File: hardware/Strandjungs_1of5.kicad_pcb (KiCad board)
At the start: 2 copper layers, 62.2 x 80.4 mm, 54 parts, among them J1 Screw_Terminal_01x02, J10 Conn_01x02, J11 Conn_01x02, J12 Conn_01x02, J2 Screw_Terminal_01x02, J3 Screw_Terminal_01x02, J4 Screw_Terminal_01x02, J5 Screw_Terminal_01x02, J6 Screw_Terminal_01x02, J7 Screw_Terminal_01x02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

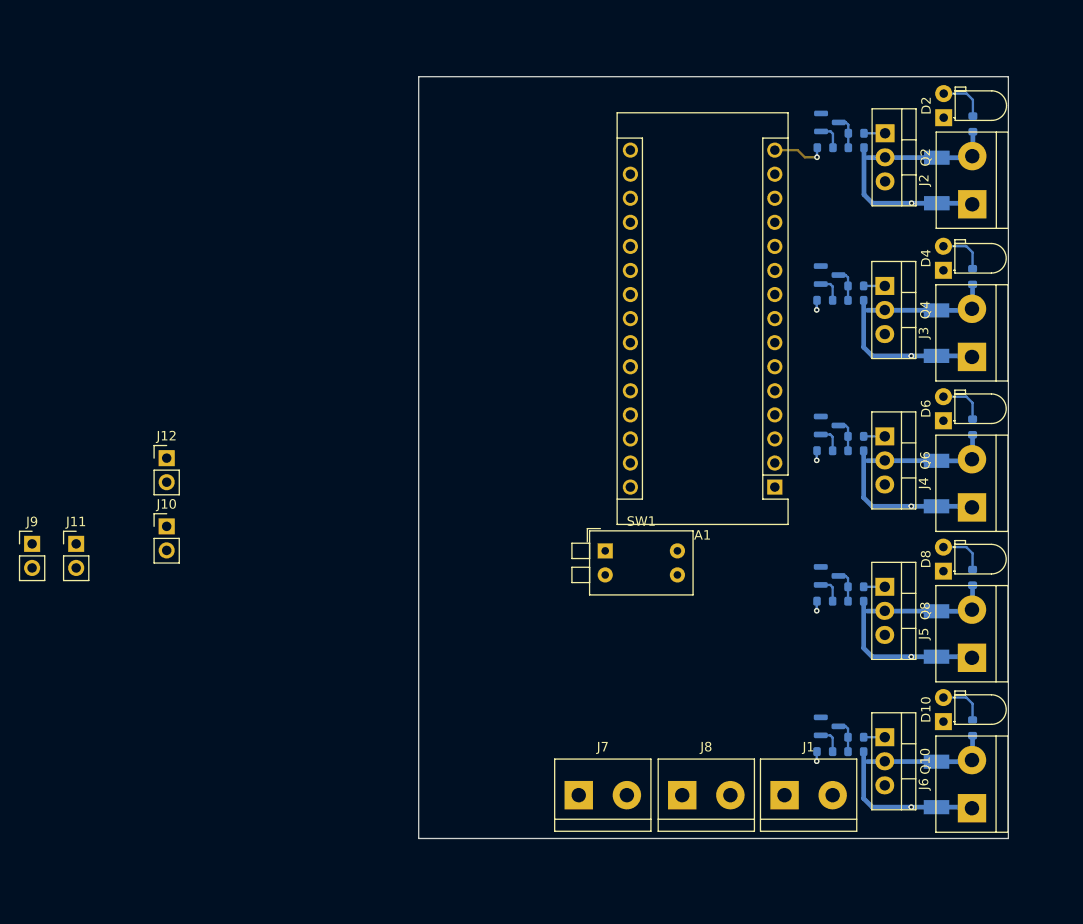
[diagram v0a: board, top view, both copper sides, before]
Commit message: first iteration of layout almost done
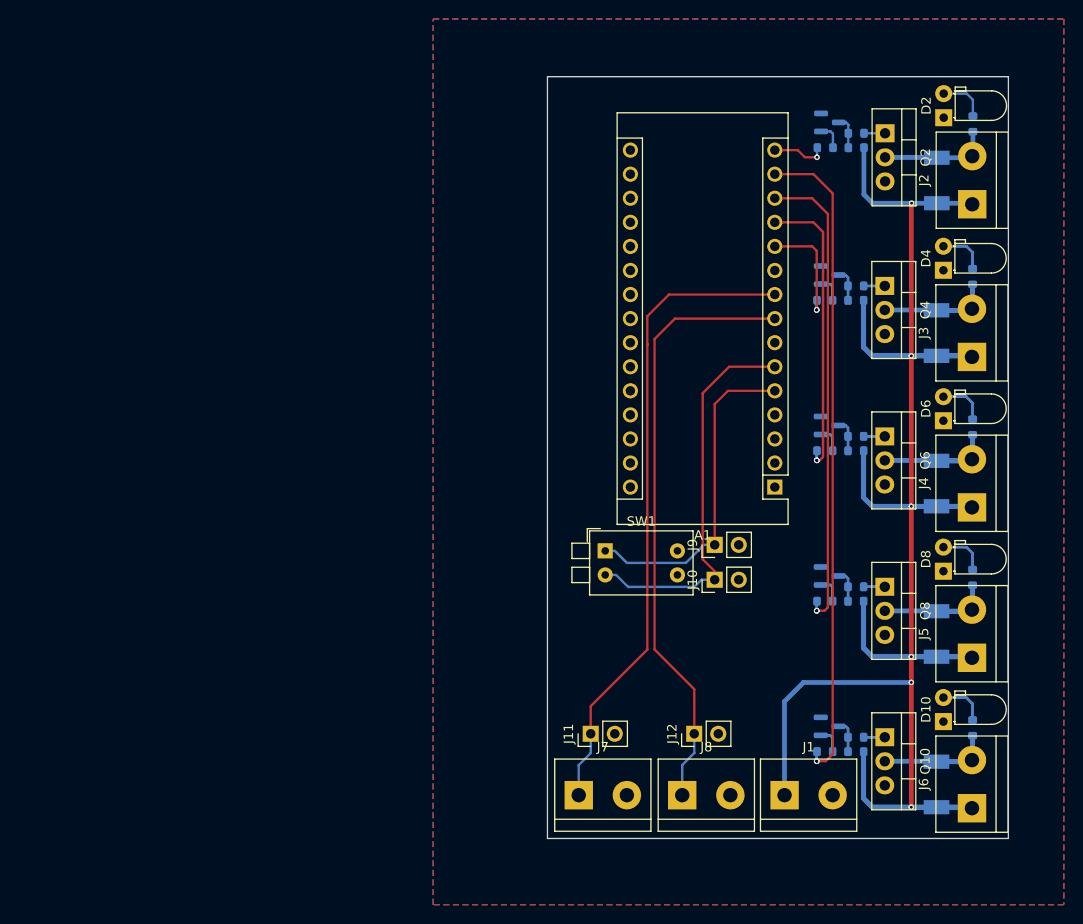
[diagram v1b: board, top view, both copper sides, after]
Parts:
- moved J9 72.0 mm to (31.6, -111.5), turned to 90 degrees
- moved J12 62.8 mm to (29.5, -91.6), turned to 90 degrees
- moved J10 58.1 mm to (31.6, -107.8), turned to 90 degrees
- moved J11 57.9 mm to (18.5, -91.6), turned to 90 degrees
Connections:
- A1 pad 8: /RESET -> /TRIGGER
- A1 pad 9: /TRIGGER -> /RESET
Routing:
- net +12V: track 0.00 -> 239.1 mm, vias 0 -> 6
- net /SWITCH4: track 1.01 -> 70.1 mm, vias 1 -> 2
- net /RESET: track 0.00 -> 68.1 mm
- net /TRIGGER: track 0.00 -> 64.0 mm
- net /SWITCH3: track 1.01 -> 51.2 mm, vias 1 -> 2
- net /SEL_1: track 0.00 -> 41.4 mm
- net /SEL_0: track 0.00 -> 34.6 mm
- net /SWITCH2: track 1.01 -> 32.1 mm, vias 1 -> 2
- net /Channel 0/MAG_RTN: track 30.5 -> 11.9 mm, vias 1 -> 0
- net /Channel 4/MAG_RTN: track 30.5 -> 18.3 mm, vias 1 -> 0
- net /Channel 3/MAG_RTN: track 30.5 -> 18.3 mm, vias 1 -> 0
- net /Channel 2/MAG_RTN: track 30.5 -> 18.3 mm, vias 1 -> 0
- net /Channel 1/MAG_RTN: track 30.5 -> 18.3 mm, vias 1 -> 0
- net /SWITCH1: track 1.01 -> 12.9 mm, vias 1 -> 2
- net Net-(D4-Pad2): track 4.94 -> 9.88 mm
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- added copper zone on B.Cu, net GND
- added copper zone on F.Cu, net GND
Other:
- board size 62.2 x 80.4 mm -> 48.6 x 80.4 mm

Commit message: added 7805 as voltage regulator
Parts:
- added R16: dnp, Resistor_SMD:R_0603_1608Metric, B.Cu at (18.9, -117.6)
- added REF**: Symbol_GNU-GPL_CopperTop_Small, Symbol:Symbol_GNU-GPL_CopperTop_Small, F.Cu at (29.2, -156.6)
- added REF**: KiCad-Logo2_6mm_SilkScreen, Symbol:KiCad-Logo2_6mm_SilkScreen, F.Cu at (42.1, -127.0)
- added U1: L7805, Package_TO_SOT_THT:TO-220-3_Vertical, F.Cu at (39.0, -96.3)
- added kibuzzard-62B9DC86: G***, kibuzzard-62B9DC86, F.Cu at (30.9, -95.1)
- added kibuzzard-62B9DCAD: G***, kibuzzard-62B9DCAD, F.Cu at (19.8, -95.2)
- added kibuzzard-62B9DCC5: G***, kibuzzard-62B9DCC5, F.Cu at (50.8, -145.8)
- added kibuzzard-62B9DCD6: G***, kibuzzard-62B9DCD6, F.Cu at (51.0, -129.7)
- added kibuzzard-62B9DCE2: G***, kibuzzard-62B9DCE2, F.Cu at (51.0, -113.8)
- added kibuzzard-62B9DCF0: G***, kibuzzard-62B9DCF0, F.Cu at (51.0, -97.8)
- added kibuzzard-62B9DD05: G***, kibuzzard-62B9DD05, F.Cu at (50.9, -82.0)
- added kibuzzard-62B9DD70: G***, kibuzzard-62B9DD70, F.Cu at (21.5, -104.1)
- moved J10 2.16 mm to (29.5, -107.7)
- moved J9 2.16 mm to (29.5, -111.4)
- moved SW1 2.16 mm to (17.9, -110.7)
- moved A1 1.14 mm to (36.8, -117.6)
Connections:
- A1 pad 27: unconnected-(A1-Pad27) -> +5V
- A1 pad 30: unconnected-(A1-Pad30) -> Net-(A1-Pad30)
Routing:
- net +5V: track 0.00 -> 39.9 mm
- net +12V: track 239.1 -> 212.2 mm
- net /Channel 1/MAG_RTN: track 18.3 -> 11.5 mm
- net /Channel 4/MAG_RTN: track 18.3 -> 11.5 mm
- net /Channel 3/MAG_RTN: track 18.3 -> 11.5 mm
- net /Channel 2/MAG_RTN: track 18.3 -> 11.5 mm
- net Net-(D4-Pad2): track 9.88 -> 4.94 mm
- net Net-(D8-Pad2): track 9.88 -> 4.94 mm
- net Net-(D6-Pad2): track 9.88 -> 4.94 mm
- net Net-(D10-Pad2): track 9.88 -> 4.94 mm
- net Net-(Q9-Pad3): track 7.05 -> 3.52 mm
- net Net-(Q5-Pad3): track 7.05 -> 3.52 mm
- net Net-(Q7-Pad3): track 7.05 -> 3.52 mm
- net Net-(Q3-Pad3): track 7.05 -> 3.52 mm
- net /TRIGGER: track 64.0 -> 67.4 mm
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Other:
- board text added: "Strandjungs Reaction Game"
- board text added: "https://github.com/JochiSt/Strandjungs_ReactionGame"

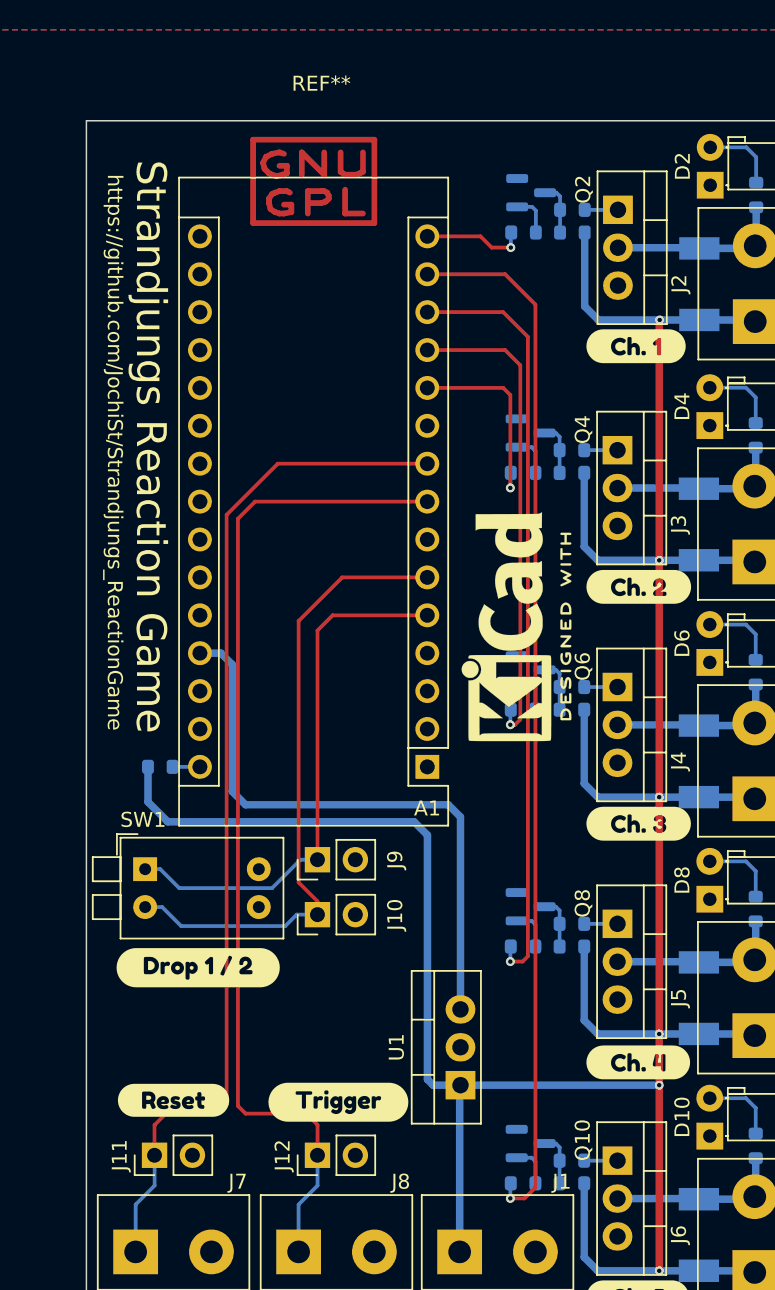
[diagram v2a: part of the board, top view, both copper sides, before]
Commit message: updated layout
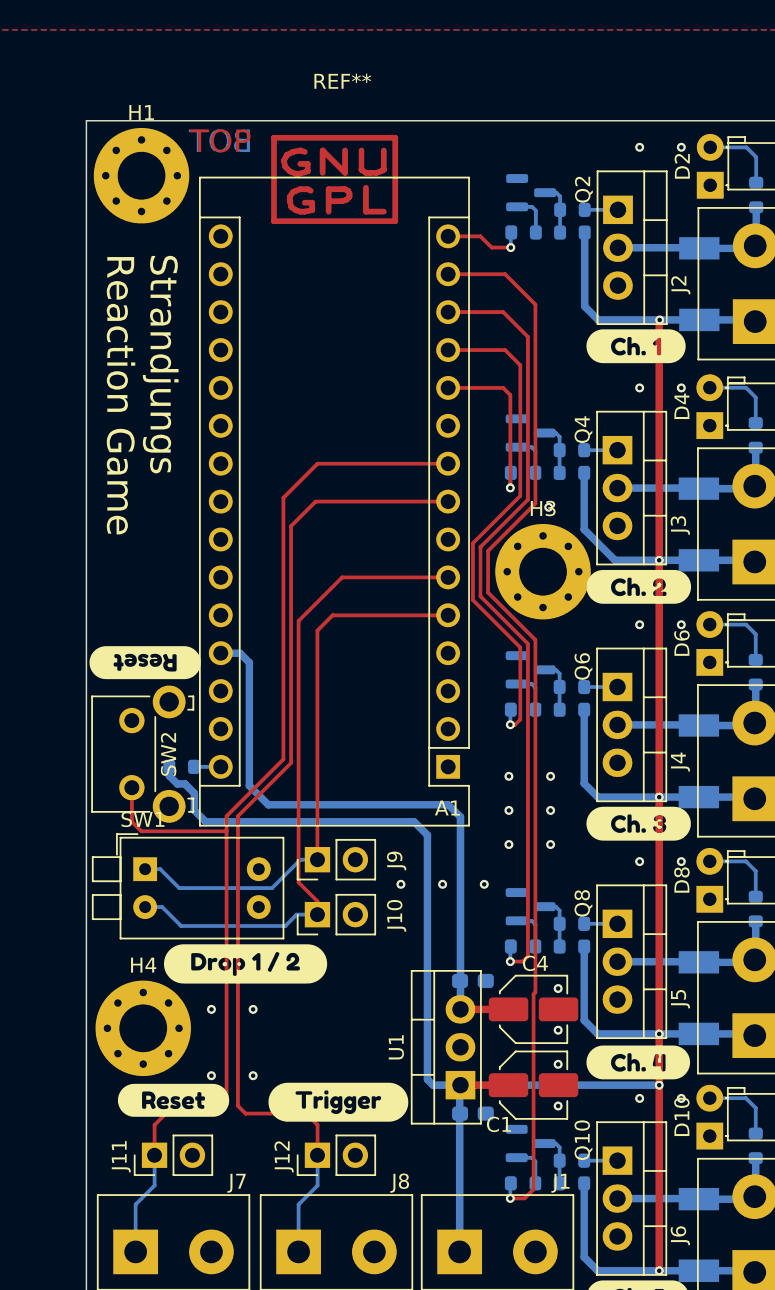
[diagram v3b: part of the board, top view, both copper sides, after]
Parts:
- added C1: 1uF, Capacitor_SMD:C_Elec_4x5.4, F.Cu at (43.9, -96.3)
- added C2: 100n, Capacitor_SMD:C_0603_1608Metric_Pad1.08x0.95mm_HandSolder, B.Cu at (39.9, -94.4)
- added C3: 100n, Capacitor_SMD:C_0603_1608Metric_Pad1.08x0.95mm_HandSolder, B.Cu at (39.9, -103.3)
- added C4: 10uF, Capacitor_SMD:C_Elec_4x5.4, F.Cu at (43.9, -101.3)
- added G***: LOGO, MadeByJochen:MadeByJochen_10x10, B.Cu at (30.9, -121.7)
- added H1: MountingHole_Pad, MountingHole:MountingHole_3.2mm_M3_Pad_Via, F.Cu at (17.7, -157.2)
- added H3: MountingHole_Pad, MountingHole:MountingHole_3.2mm_M3_Pad_Via, F.Cu at (44.6, -130.7)
- added H4: MountingHole_Pad, MountingHole:MountingHole_3.2mm_M3_Pad_Via, F.Cu at (17.8, -100.1)
- added SW2: SW_Push, Button_Switch_THT:SW_Tactile_SKHH_Angled, F.Cu at (17.0, -116.2)
- added kibuzzard-62B9DCAD: G***, kibuzzard-62B9DCAD, F.Cu at (17.9, -124.6)
- REF**: moved to B.Cu
- moved REF** 22.6 mm to (31.6, -146.9)
- moved kibuzzard-62B9DD70 3.19 mm to (24.6, -104.4)
- moved R16 1.43 mm to (20.4, -117.6)
- moved REF** 1.40 mm to (30.6, -156.7)
- moved A1 1.40 mm to (38.2, -117.6)
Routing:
- net /RESET: track 68.7 -> 77.5 mm
- net +5V: track 39.9 -> 41.6 mm
- net /SEL_0: track 35.9 -> 37.4 mm
- net /SWITCH1: track 13.0 -> 11.6 mm
- net /SWITCH0: track 6.92 -> 5.52 mm
- net /SEL_1: track 42.4 -> 43.8 mm
- net /SWITCH4: track 70.3 -> 71.5 mm
- net /SWITCH2: track 32.2 -> 33.5 mm
- net /SWITCH3: track 51.3 -> 52.5 mm
- net /TRIGGER: track 67.4 -> 66.4 mm
- net +12V: track 212.2 -> 212.9 mm
- net GND: vias 0 -> 28
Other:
- board text added: "BOT"
- board text added: "JS 06/2022"
- board text added: "TOP"

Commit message: updated AISLER project ID
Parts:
- moved A1 236.6 mm to (151.2, 90.3)
- moved C1 236.6 mm to (156.9, 111.6)
- moved C2 236.6 mm to (152.8, 113.5)
- moved C3 236.6 mm to (152.8, 104.6)
- moved C4 236.6 mm to (156.9, 106.6)
- moved D1 236.6 mm to (168.0, 57.9)
- moved D10 236.6 mm to (168.7, 115.0)
- moved D2 236.6 mm to (168.8, 51.3)
- moved D3 236.6 mm to (168.0, 74.1)
- moved D4 236.6 mm to (168.7, 67.4)
- moved D5 236.6 mm to (168.0, 89.9)
- moved D6 236.6 mm to (168.7, 83.3)
- moved D7 236.6 mm to (168.0, 105.8)
- moved D8 236.6 mm to (168.7, 99.2)
- moved D9 236.6 mm to (168.0, 121.7)
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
